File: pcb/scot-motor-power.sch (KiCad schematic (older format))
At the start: 18 parts, among them U11 MCP1703A-3302_SOT223, U6 TSR_1-2465, U7 INA260, U8 MCP1703A-3302_SOT223, U9 MCP1703A-5002_SOT223

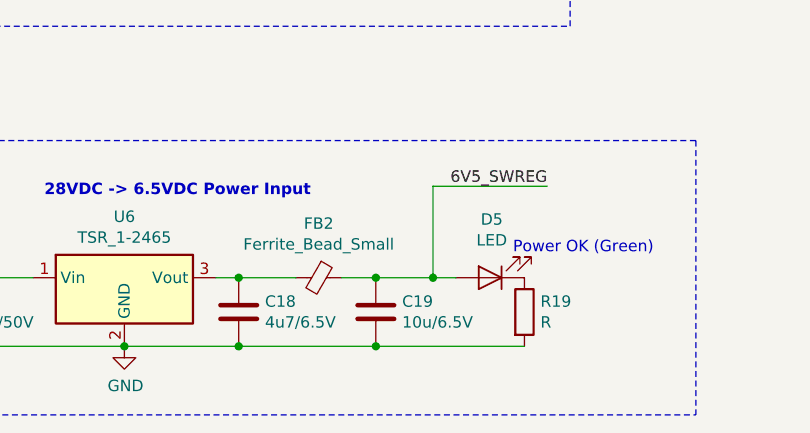
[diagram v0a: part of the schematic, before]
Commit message: pcb: Add BOM list. Adjust some values to reduce lines.
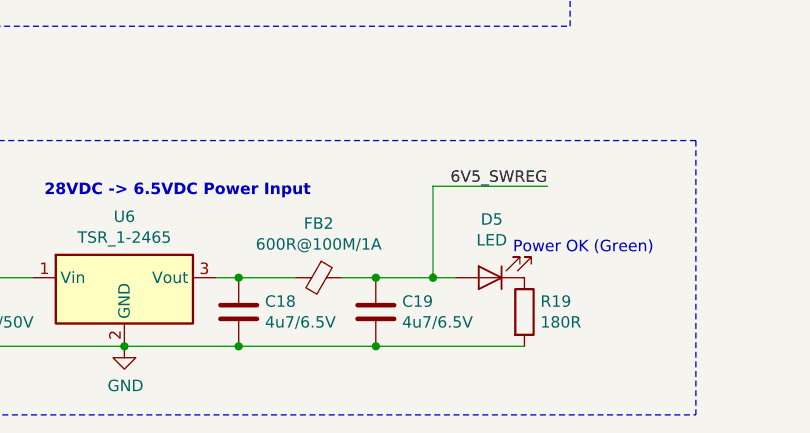
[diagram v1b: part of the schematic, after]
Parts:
- C19: value 10u/6.5V -> 4u7/6.5V
- FB2: value Ferrite_Bead_Small -> 600R@100M/1A
- R19: value R -> 180R
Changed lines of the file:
@@
 P 5100 5100
 F 0 "FB2" V 4863 5100 50  0000 C CNN
-F 1 "Ferrite_Bead_Small" V 4954 5100 50  0000 C CNN
+F 1 "600R@100M/1A" V 4954 5100 50  0000 C CNN
 F 2 "Inductor_SMD:L_0805_2012Metric_Pad1.15x1.40mm_HandSolder" V 5030 5100 50  0001 C CNN
 F 3 "~" H 5100 5100 50  0001 C CNN
@@
 P 5350 5250
 F 0 "C19" H 5465 5296 50  0000 L CNN
-F 1 "10u/6.5V" H 5465 5205 50  0000 L CNN
+F 1 "4u7/6.5V" H 5465 5205 50  0000 L CNN
 F 2 "Capacitor_SMD:C_0805_2012Metric_Pad1.15x1.40mm_HandSolder" H 5388 5100 50  0001 C CNN
 F 3 "~" H 5350 5250 50  0001 C CNN
@@
 P 6000 5250
 F 0 "R19" H 6070 5296 50  0000 L CNN
-F 1 "R" H 6070 5205 50  0000 L CNN
+F 1 "180R" H 6070 5205 50  0000 L CNN
 F 2 "Resistor_SMD:R_0805_2012Metric_Pad1.15x1.40mm_HandSolder" V 5930 5250 50  0001 C CNN
 F 3 "~" H 6000 5250 50  0001 C CNN
